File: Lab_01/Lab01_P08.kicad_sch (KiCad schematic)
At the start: 3 parts

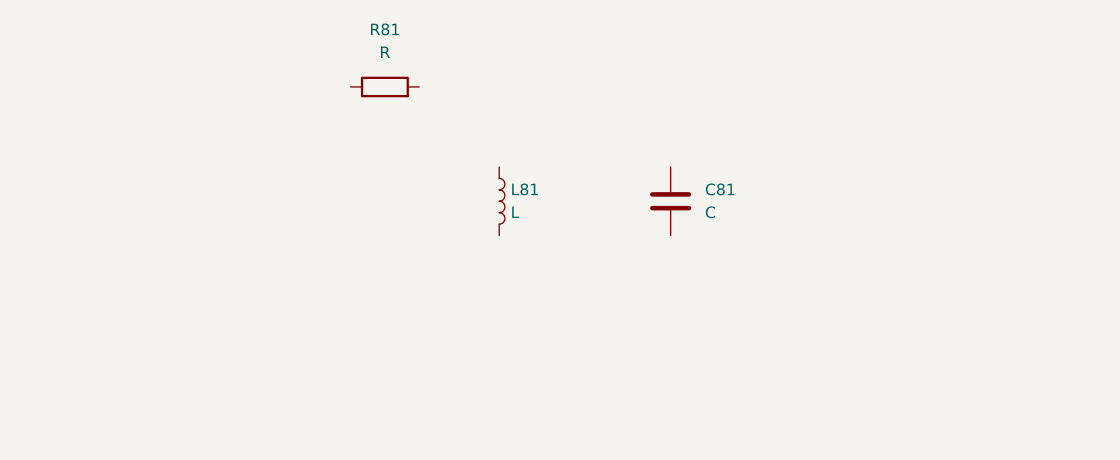
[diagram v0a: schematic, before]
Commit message: Simulate Problem 8
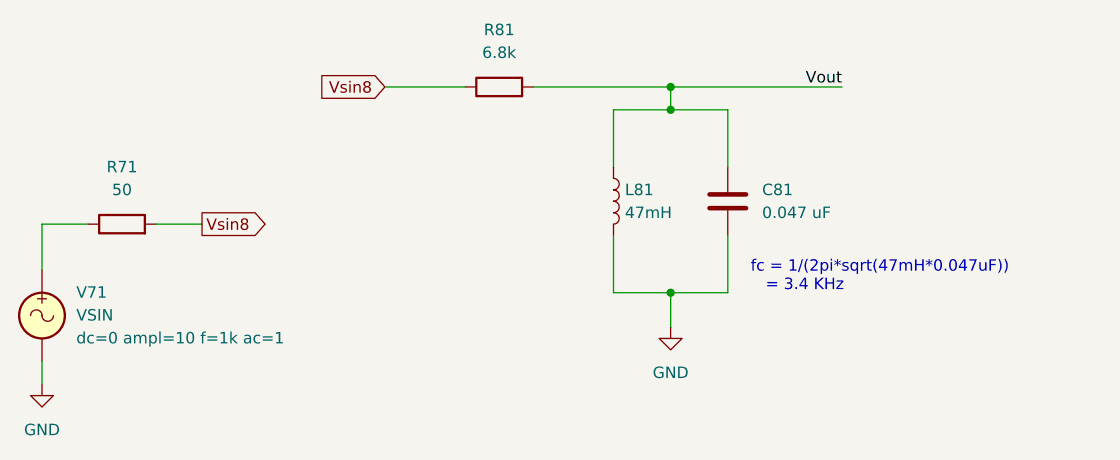
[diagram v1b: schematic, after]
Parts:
- added R71: 50, symbol Device:R
- added V71: VSIN, symbol Simulation_SPICE:VSIN
- C81: value C -> 0.047 uF
- L81: value L -> 47mH
- R81: value R -> 6.8k
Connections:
- net Vsin8: now reaches R81.1
- net Vsin8: now also R71.2
- net Vout: now reaches R81.2
- net Vout: now also C81.1, L81.1
- net GND: now reaches C81.2
- net GND: now also L81.2, V71.2
- new net: R71.1, V71.1
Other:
- note added: "fc = 1/(2pi*sqrt(47mH*0.047uF)) = 3.4 KHz"
- moved on the sheet: C81, L81, R81
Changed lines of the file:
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@@
     (date "2024-01-24")
   )
-  (symbol (lib_id "Device:R") (at 63.5 38.1 90) (unit 1)
-    (in_bom yes) (on_board yes) (dnp no) (fields_autoplaced)
-    (property "Reference" "R81" (at 63.5 31.75 90)
-      (effects (font (size 1.27 1.27)))
-    )
-    (property "Value" "R" (at 63.5 34.29 90)
-      (effects (font (size 1.27 1.27)))
-    )
-    (property "Footprint" "" (at 63.5 39.878 90)
-      (effects (font (size 1.27 1.27)) hide)
-    )
-    (property "Datasheet" "~" (at 63.5 38.1 0)
+  (junction (at 95.25 40.64) (diameter 0) (color 0 0 0 0)
+  )
+  (junction (at 95.25 60.96) (diameter 0) (color 0 0 0 0)
+  )
+  (junction (at 95.25 38.1) (diameter 0) (color 0 0 0 0)
+  )
+  (wire (pts (xy 95.25 60.96) (xy 101.6 60.96))
+    (stroke (width 0) (type default))
+  )
+  (wire (pts (xy 25.4 68.58) (xy 25.4 71.12))
+    (stroke (width 0) (type default))
+  )
+  (wire (pts (xy 88.9 40.64) (xy 88.9 46.99))
+    (stroke (width 0) (type default))
+  )
+  (wire (pts (xy 25.4 53.34) (xy 25.4 58.42))
+    (stroke (width 0) (type default))
+  )
+  (wire (pts (xy 95.25 38.1) (xy 95.25 40.64))
+    (stroke (width 0) (type default))
+  )
+  (wire (pts (xy 101.6 54.61) (xy 101.6 60.96))
+    (stroke (width 0) (type default))
+  )
+  (wire (pts (xy 30.48 53.34) (xy 25.4 53.34))
+    (stroke (width 0) (type default))
+  )
+  (wire (pts (xy 63.5 38.1) (xy 72.39 38.1))
+    (stroke (width 0) (type default))
+  )
+  (wire (pts (xy 95.25 60.96) (xy 88.9 60.96))
+    (stroke (width 0) (type default))
+  )
+  (wire (pts (xy 95.25 60.96) (xy 95.25 64.77))
+    (stroke (width 0) (type default))
+  )
+  (wire (pts (xy 101.6 46.99) (xy 101.6 40.64))
+    (stroke (width 0) (type default))
+  )
+  (wire (pts (xy 95.25 40.64) (xy 101.6 40.64))
+    (stroke (width 0) (type default))
+  )
+  (wire (pts (xy 80.01 38.1) (xy 95.25 38.1))
+    (stroke (width 0) (type default))
+  )
+  (wire (pts (xy 88.9 60.96) (xy 88.9 54.61))
+    (stroke (width 0) (type default))
+  )
+  (wire (pts (xy 95.25 38.1) (xy 114.3 38.1))
+    (stroke (width 0) (type default))
+  )
+  (wire (pts (xy 38.1 53.34) (xy 43.18 53.34))
+    (stroke (width 0) (type default))
+  )
+  (wire (pts (xy 88.9 40.64) (xy 95.25 40.64))
+    (stroke (width 0) (type default))
+  )
+  (text "fc = 1/(2pi*sqrt(47mH*0.047uF))\n   = 3.4 KHz" (at 104.14 60.96 0)
+    (effects (font (size 1.27 1.27)) (justify left bottom))
+  )
+  (label "Vout" (at 114.3 38.1 180) (fields_autoplaced)
+    (effects (font (size 1.27 1.27)) (justify right bottom))
+  )
+  (global_label "Vsin8" (shape input) (at 63.5 38.1 180) (fields_autoplaced)
+    (effects (font (size 1.27 1.27)) (justify right))
+    (property "Intersheetrefs" "${INTERSHEET_REFS}" (at 55.5142 38.1 0)
+      (effects (font (size 1.27 1.27)) (justify right) hide)
+    )
+  )
+  (global_label "Vsin8" (shape output) (at 43.18 53.34 0) (fields_autoplaced)
+    (effects (font (size 1.27 1.27)) (justify left))
+    (property "Intersheetrefs" "${INTERSHEET_REFS}" (at 51.1658 53.34 0)
+      (effects (font (size 1.27 1.27)) (justify left) hide)
+    )
+  )
+  (symbol (lib_id "Device:R") (at 76.2 38.1 90) (unit 1)
+    (in_bom yes) (on_board yes) (dnp no) (fields_autoplaced)
+    (property "Reference" "R81" (at 76.2 31.75 90)
+      (effects (font (size 1.27 1.27)))
+    )
+    (property "Value" "6.8k" (at 76.2 34.29 90)
+      (effects (font (size 1.27 1.27)))
+    )
+    (property "Footprint" "" (at 76.2 39.878 90)
+      (effects (font (size 1.27 1.27)) hide)
+    )
+    (property "Datasheet" "~" (at 76.2 38.1 0)
       (effects (font (size 1.27 1.27)) hide)
     )
@@
     )
   )
-  (symbol (lib_id "Device:C") (at 95.25 50.8 0) (unit 1)
-    (in_bom yes) (on_board yes) (dnp no) (fields_autoplaced)
-    (property "Reference" "C81" (at 99.06 49.53 0)
-      (effects (font (size 1.27 1.27)) (justify left))
-    )
-    (property "Value" "C" (at 99.06 52.07 0)
-      (effects (font (size 1.27 1.27)) (justify left))
-    )
-    (property "Footprint" "" (at 96.2152 54.61 0)
-      (effects (font (size 1.27 1.27)) hide)
-    )
-    (property "Datasheet" "~" (at 95.25 50.8 0)
+  (symbol (lib_id "power:GND") (at 25.4 71.12 0) (unit 1)
+    (in_bom yes) (on_board yes) (dnp no) (fields_autoplaced)
+    (property "Reference" "#PWR09" (at 25.4 77.47 0)
+      (effects (font (size 1.27 1.27)) hide)
+    )
+    (property "Value" "GND" (at 25.4 76.2 0)
+      (effects (font (size 1.27 1.27)))
+    )
+    (property "Footprint" "" (at 25.4 71.12 0)
+      (effects (font (size 1.27 1.27)) hide)
+    )
+    (property "Datasheet" "" (at 25.4 71.12 0)
+      (effects (font (size 1.27 1.27)) hide)
+    )
+    (pin "1")
+    (instances
+      (project "Lab01"
+        (path "/f5e37932-d66b-45bd-afc2-f24a1a74700d/07e6c46f-635f-421c-8ccf-3318813d28b5"
+          (reference "#PWR09") (unit 1)
+        )
+        (path "/f5e37932-d66b-45bd-afc2-f24a1a74700d/4af23c30-41c4-4fc2-b482-07e0e5856a6e"
+          (reference "#PWR011") (unit 1)
+        )
+      )
+    )
+  )
+  (symbol (lib_id "Device:C") (at 101.6 50.8 0) (unit 1)
+    (in_bom yes) (on_board yes) (dnp no) (fields_autoplaced)
+    (property "Reference" "C81" (at 105.41 49.53 0)
+      (effects (font (size 1.27 1.27)) (justify left))
+    )
+    (property "Value" "0.047 uF" (at 105.41 52.07 0)
+      (effects (font (size 1.27 1.27)) (justify left))
+    )
+    (property "Footprint" "" (at 102.5652 54.61 0)
+      (effects (font (size 1.27 1.27)) hide)
+    )
+    (property "Datasheet" "~" (at 101.6 50.8 0)
       (effects (font (size 1.27 1.27)) hide)
     )
@@
     )
   )
-  (symbol (lib_id "Device:L") (at 76.2 50.8 0) (unit 1)
-    (in_bom yes) (on_board yes) (dnp no) (fields_autoplaced)
-    (property "Reference" "L81" (at 77.47 49.53 0)
-      (effects (font (size 1.27 1.27)) (justify left))
-    )
-    (property "Value" "L" (at 77.47 52.07 0)
-      (effects (font (size 1.27 1.27)) (justify left))
-    )
-    (property "Footprint" "" (at 76.2 50.8 0)
-      (effects (font (size 1.27 1.27)) hide)
-    )
-    (property "Datasheet" "~" (at 76.2 50.8 0)
-      (effects (font (size 1.27 1.27)) hide)
-    )
+  (symbol (lib_id "Device:R") (at 34.29 53.34 90) (unit 1)
+    (in_bom yes) (on_board yes) (dnp no) (fields_autoplaced)
+    (property "Reference" "R71" (at 34.29 46.99 90)
+      (effects (font (size 1.27 1.27)))
+    )
+    (property "Value" "50" (at 34.29 49.53 90)
+      (effects (font (size 1.27 1.27)))
+    )
+    (property "Footprint" "" (at 34.29 55.118 90)
+      (effects (font (size 1.27 1.27)) hide)
+    )
+    (property "Datasheet" "~" (at 34.29 53.34 0)
+      (effects (font (size 1.27 1.27)) hide)
+    )
+    (pin "1")
+    (pin "2")
+    (instances
+      (project "Lab01"
+        (path "/f5e37932-d66b-45bd-afc2-f24a1a74700d/07e6c46f-635f-421c-8ccf-3318813d28b5"
+          (reference "R71") (unit 1)
+        )
+        (path "/f5e37932-d66b-45bd-afc2-f24a1a74700d/4af23c30-41c4-4fc2-b482-07e0e5856a6e"
+          (reference "R2") (unit 1)
+        )
+      )
+    )
+  )
+  (symbol (lib_id "Simulation_SPICE:VSIN") (at 25.4 63.5 0) (unit 1)
+    (in_bom yes) (on_board yes) (dnp no) (fields_autoplaced)
+    (property "Reference" "V71" (at 29.21 60.9242 0)
+      (effects (font (size 1.27 1.27)) (justify left))
+    )
+    (property "Value" "VSIN" (at 29.21 63.4642 0)
+      (effects (font (size 1.27 1.27)) (justify left))
+    )
+    (property "Footprint" "" (at 25.4 63.5 0)
+      (effects (font (size 1.27 1.27)) hide)
+    )
+    (property "Datasheet" "~" (at 25.4 63.5 0)
+      (effects (font (size 1.27 1.27)) hide)
+    )
+    (property "Sim.Pins" "1=+ 2=-" (at 25.4 63.5 0)
+      (effects (font (size 1.27 1.27)) hide)
+    )
+    (property "Sim.Params" "dc=0 ampl=10 f=1k ac=1" (at 29.21 66.0042 0)
+      (effects (font (size 1.27 1.27)) (justify left))
+    )
+    (property "Sim.Type" "SIN" (at 25.4 63.5 0)
+      (effects (font (size 1.27 1.27)) hide)
+    )
+    (property "Sim.Device" "V" (at 25.4 63.5 0)
+      (effects (font (size 1.27 1.27)) (justify left) hide)
+    )
+    (pin "1")
+    (pin "2")
+    (instances
+      (project "Lab01"
+        (path "/f5e37932-d66b-45bd-afc2-f24a1a74700d/07e6c46f-635f-421c-8ccf-3318813d28b5"
+          (reference "V71") (unit 1)
+        )
+        (path "/f5e37932-d66b-45bd-afc2-f24a1a74700d/4af23c30-41c4-4fc2-b482-07e0e5856a6e"
+          (reference "V81") (unit 1)
+        )
+      )
+    )
+  )
+  (symbol (lib_id "power:GND") (at 95.25 64.77 0) (unit 1)
+    (in_bom yes) (on_board yes) (dnp no) (fields_autoplaced)
+    (property "Reference" "#PWR09" (at 95.25 71.12 0)
+      (effects (font (size 1.27 1.27)) hide)
+    )
+    (property "Value" "GND" (at 95.25 69.85 0)
+      (effects (font (size 1.27 1.27)))
+    )
+    (property "Footprint" "" (at 95.25 64.77 0)
+      (effects (font (size 1.27 1.27)) hide)
+    )
+    (property "Datasheet" "" (at 95.25 64.77 0)
+      (effects (font (size 1.27 1.27)) hide)
+    )
+    (pin "1")
+    (instances
+      (project "Lab01"
+        (path "/f5e37932-d66b-45bd-afc2-f24a1a74700d/07e6c46f-635f-421c-8ccf-3318813d28b5"
+          (reference "#PWR09") (unit 1)
+        )
+        (path "/f5e37932-d66b-45bd-afc2-f24a1a74700d/4af23c30-41c4-4fc2-b482-07e0e5856a6e"
+          (reference "#PWR012") (unit 1)
+        )
+      )
+    )
+  )
+  (symbol (lib_id "Device:L") (at 88.9 50.8 0) (unit 1)
+    (in_bom yes) (on_board yes) (dnp no) (fields_autoplaced)
+    (property "Reference" "L81" (at 90.17 49.53 0)
+      (effects (font (size 1.27 1.27)) (justify left))
+    )
+    (property "Value" "47mH" (at 90.17 52.07 0)
+      (effects (font (size 1.27 1.27)) (justify left))
+    )
+    (property "Footprint" "" (at 88.9 50.8 0)
+      (effects (font (size 1.27 1.27)) hide)
+    )
+    (property "Datasheet" "~" (at 88.9 50.8 0)
+      (effects (font (size 1.27 1.27)) hide)
+    )

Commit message: Update Lab 01 Problem 8 schematic
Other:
- company: (none) -> Jim Horwitz & Mark Vaughn, Jork Incorporated
- title: (none) -> Parallel Resonant Filter
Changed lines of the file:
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@@
   (paper "User" 177.8 127)
   (title_block
+    (title "Parallel Resonant Filter")
     (date "2024-01-24")
+    (rev "0")
+    (company "Jim Horwitz & Mark Vaughn, Jork Incorporated")
   )
   (junction (at 95.25 40.64) (diameter 0) (color 0 0 0 0)

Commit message: Finish Lab 01
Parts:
- R81: value 6.8k -> 68k
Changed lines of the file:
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@@
       (effects (font (size 1.27 1.27)))
     )
-    (property "Value" "6.8k" (at 76.2 34.29 90)
+    (property "Value" "68k" (at 76.2 34.29 90)
       (effects (font (size 1.27 1.27)))
     )
